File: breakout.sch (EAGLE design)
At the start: 5 parts

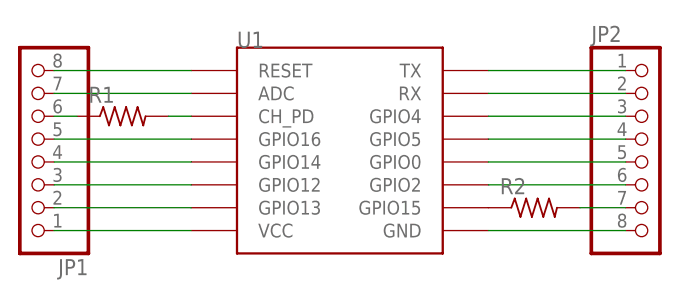
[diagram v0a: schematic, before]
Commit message: Added GPIO0 resistor
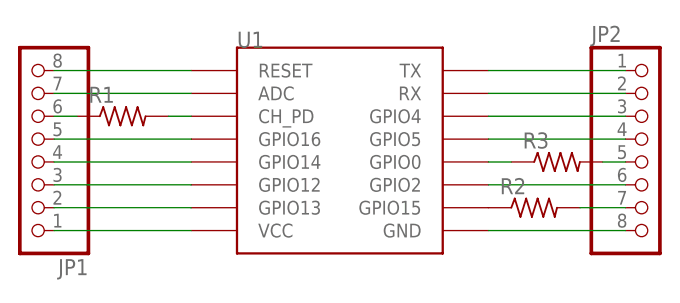
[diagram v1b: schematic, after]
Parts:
- added R3: (no value), resistor:R-US_R0805
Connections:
- new net N$19: JP2.5, R3.2
- net N$13: now also R3.1; no longer JP2.5
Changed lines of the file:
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@@
 <part name="R1" library="resistor" deviceset="R-US_" device="R0805"/>
 <part name="R2" library="resistor" deviceset="R-US_" device="R0805"/>
+<part name="R3" library="resistor" deviceset="R-US_" device="R0805"/>
 </parts>
 <sheets>
@@
 <attribute name="NAME" x="72.39" y="44.6786" size="1.778" layer="95"/>
 <attribute name="VALUE" x="72.39" y="39.878" size="1.778" layer="96"/>
+</instance>
+<instance part="R3" gate="G$1" x="78.74" y="48.26">
+<attribute name="NAME" x="74.93" y="49.7586" size="1.778" layer="95"/>
+<attribute name="VALUE" x="74.93" y="44.958" size="1.778" layer="96"/>
 </instance>
 </instances>
@@
 </segment>
 </net>
-<net name="N$13" class="0">
-<segment>
-<pinref part="U1" gate="G$1" pin="GPIO0"/>
-<pinref part="JP2" gate="A" pin="5"/>
-<wire x1="86.36" y1="48.26" x2="71.12" y2="48.26" width="0.1524" layer="91"/>
-</segment>
-</net>
 <net name="N$14" class="0">
 <segment>
@@
 </segment>
 </net>
+<net name="N$13" class="0">
+<segment>
+<pinref part="U1" gate="G$1" pin="GPIO0"/>
+<pinref part="R3" gate="G$1" pin="1"/>
+<wire x1="73.66" y1="48.26" x2="71.12" y2="48.26" width="0.1524" layer="91"/>
+</segment>
+</net>
+<net name="N$19" class="0">
+<segment>
+<pinref part="JP2" gate="A" pin="5"/>
+<pinref part="R3" gate="G$1" pin="2"/>
+<wire x1="83.82" y1="48.26" x2="86.36" y2="48.26" width="0.1524" layer="91"/>
+</segment>
+</net>

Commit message: Modified pads, changed traces width and gcode options
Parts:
- JP1, JP2: device pinhead:PINHD-1X8 -> pinhead-1:PINHD-1X8_2.54
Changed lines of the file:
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@@
 <grid distance="0.1" unitdist="inch" unit="inch" style="lines" multiple="1" display="no" altdistance="0.01" altunitdist="inch" altunit="inch"/>
 <layers>
-<layer number="1" name="Top" color="4" fill="1" visible="no" active="no"/>
-<layer number="2" name="Route2" color="1" fill="3" visible="no" active="no"/>
-<layer number="3" name="Route3" color="4" fill="3" visible="no" active="no"/>
-<layer number="4" name="Route4" color="1" fill="4" visible="no" active="no"/>
-<layer number="5" name="Route5" color="4" fill="4" visible="no" active="no"/>
-<layer number="6" name="Route6" color="1" fill="8" visible="no" active="no"/>
-<layer number="7" name="Route7" color="4" fill="8" visible="no" active="no"/>
-<layer number="8" name="Route8" color="1" fill="2" visible="no" active="no"/>
-<layer number="9" name="Route9" color="4" fill="2" visible="no" active="no"/>
-<layer number="10" name="Route10" color="1" fill="7" visible="no" active="no"/>
-<layer number="11" name="Route11" color="4" fill="7" visible="no" active="no"/>
-<layer number="12" name="Route12" color="1" fill="5" visible="no" active="no"/>
-<layer number="13" name="Route13" color="4" fill="5" visible="no" active="no"/>
-<layer number="14" name="Route14" color="1" fill="6" visible="no" active="no"/>
-<layer number="15" name="Route15" color="4" fill="6" visible="no" active="no"/>
-<layer number="16" name="Bottom" color="1" fill="1" visible="no" active="no"/>
-<layer number="17" name="Pads" color="2" fill="1" visible="no" active="no"/>
-<layer number="18" name="Vias" color="2" fill="1" visible="no" active="no"/>
-<layer number="19" name="Unrouted" color="6" fill="1" visible="no" active="no"/>
-<layer number="20" name="Dimension" color="15" fill="1" visible="no" active="no"/>
-<layer number="21" name="tPlace" color="7" fill="1" visible="no" active="no"/>
-<layer number="22" name="bPlace" color="7" fill="1" visible="no" active="no"/>
-<layer number="23" name="tOrigins" color="15" fill="1" visible="no" active="no"/>
-<layer number="24" name="bOrigins" color="15" fill="1" visible="no" active="no"/>
-<layer number="25" name="tNames" color="7" fill="1" visible="no" active="no"/>
-<layer number="26" name="bNames" color="7" fill="1" visible="no" active="no"/>
-<layer number="27" name="tValues" color="7" fill="1" visible="no" active="no"/>
-<layer number="28" name="bValues" color="7" fill="1" visible="no" active="no"/>
+<layer number="1" name="Top" color="4" fill="1" visible="yes" active="no"/>
+<layer number="2" name="Route2" color="16" fill="1" visible="yes" active="no"/>
+<layer number="3" name="Route3" color="17" fill="1" visible="yes" active="no"/>
+<layer number="4" name="Route4" color="18" fill="1" visible="yes" active="no"/>
+<layer number="5" name="Route5" color="19" fill="1" visible="yes" active="no"/>
+<layer number="6" name="Route6" color="25" fill="1" visible="yes" active="no"/>
+<layer number="7" name="Route7" color="26" fill="1" visible="yes" active="no"/>
+<layer number="8" name="Route8" color="27" fill="1" visible="yes" active="no"/>
+<layer number="9" name="Route9" color="28" fill="1" visible="yes" active="no"/>
+<layer number="10" name="Route10" color="29" fill="1" visible="yes" active="no"/>
+<layer number="11" name="Route11" color="30" fill="1" visible="yes" active="no"/>
+<layer number="12" name="Route12" color="20" fill="1" visible="yes" active="no"/>
+<layer number="13" name="Route13" color="21" fill="1" visible="yes" active="no"/>
+<layer number="14" name="Route14" color="22" fill="1" visible="yes" active="no"/>
+<layer number="15" name="Route15" color="23" fill="1" visible="yes" active="no"/>
+<layer number="16" name="Bottom" color="1" fill="1" visible="yes" active="no"/>
+<layer number="17" name="Pads" color="2" fill="1" visible="yes" active="no"/>
+<layer number="18" name="Vias" color="2" fill="1" visible="yes" active="no"/>
+<layer number="19" name="Unrouted" color="6" fill="1" visible="yes" active="no"/>
+<layer number="20" name="Dimension" color="24" fill="1" visible="yes" active="no"/>
+<layer number="21" name="tPlace" color="7" fill="1" visible="yes" active="no"/>
+<layer number="22" name="bPlace" color="7" fill="1" visible="yes" active="no"/>
+<layer number="23" name="tOrigins" color="15" fill="1" visible="yes" active="no"/>
+<layer number="24" name="bOrigins" color="15" fill="1" visible="yes" active="no"/>
+<layer number="25" name="tNames" color="7" fill="1" visible="yes" active="no"/>
+<layer number="26" name="bNames" color="7" fill="1" visible="yes" active="no"/>
+<layer number="27" name="tValues" color="7" fill="1" visible="yes" active="no"/>
+<layer number="28" name="bValues" color="7" fill="1" visible="yes" active="no"/>
 <layer number="29" name="tStop" color="7" fill="3" visible="no" active="no"/>
 <layer number="30" name="bStop" color="7" fill="6" visible="no" active="no"/>
@@
 <layer number="35" name="tGlue" color="7" fill="4" visible="no" active="no"/>
 <layer number="36" name="bGlue" color="7" fill="5" visible="no" active="no"/>
-<layer number="37" name="tTest" color="7" fill="1" visible="no" active="no"/>
-<layer number="38" name="bTest" color="7" fill="1" visible="no" active="no"/>
+<layer number="37" name="tTest" color="7" fill="1" visible="yes" active="no"/>
+<layer number="38" name="bTest" color="7" fill="1" visible="yes" active="no"/>
 <layer number="39" name="tKeepout" color="4" fill="11" visible="no" active="no"/>
 <layer number="40" name="bKeepout" color="1" fill="11" visible="no" active="no"/>
@@
 <layer number="44" name="Drills" color="7" fill="1" visible="no" active="no"/>
 <layer number="45" name="Holes" color="7" fill="1" visible="no" active="no"/>
-<layer number="46" name="Milling" color="3" fill="1" visible="no" active="no"/>
-<layer number="47" name="Measures" color="7" fill="1" visible="no" active="no"/>
-<layer number="48" name="Document" color="7" fill="1" visible="no" active="no"/>
-<layer number="49" name="Reference" color="7" fill="1" visible="no" active="no"/>
-<layer number="51" name="tDocu" color="7" fill="1" visible="no" active="no"/>
-<layer number="52" name="bDocu" color="7" fill="1" visible="no" active="no"/>
+<layer number="46" name="Milling" color="3" fill="1" visible="yes" active="no"/>
+<layer number="47" name="Measures" color="7" fill="1" visible="yes" active="no"/>
+<layer number="48" name="Document" color="7" fill="1" visible="yes" active="no"/>
+<layer number="49" name="Reference" color="7" fill="1" visible="yes" active="no"/>
+<layer number="51" name="tDocu" color="7" fill="1" visible="yes" active="no"/>
+<layer number="52" name="bDocu" color="7" fill="1" visible="yes" active="no"/>
 <layer number="88" name="SimResults" color="9" fill="1" visible="yes" active="yes"/>
 <layer number="89" name="SimProbes" color="9" fill="1" visible="yes" active="yes"/>
@@
 <parts>
 <part name="U1" library="esp8266modules" deviceset="ESP12" device="SMD"/>
-<part name="JP1" library="pinhead" library_urn="urn:adsk.eagle:library:325" deviceset="PINHD-1X8" device="" package3d_urn="urn:adsk.eagle:package:22409/2"/>
-<part name="JP2" library="pinhead" library_urn="urn:adsk.eagle:library:325" deviceset="PINHD-1X8" device="" package3d_urn="urn:adsk.eagle:package:22409/2"/>
+<part name="JP1" library="pinhead-1" deviceset="PINHD-1X8" device="_2.54"/>
+<part name="JP2" library="pinhead-1" deviceset="PINHD-1X8" device="_2.54"/>
 <part name="R1" library="resistor" deviceset="R-US_" device="R0805"/>
 <part name="R2" library="resistor" deviceset="R-US_" device="R0805"/>
@@
 </segment>
 </net>
-<net name="N$6" class="0">
-<segment>
-<pinref part="JP2" gate="A" pin="7"/>
-<wire x1="86.36" y1="43.18" x2="81.28" y2="43.18" width="0.1524" layer="91"/>
-<pinref part="R2" gate="G$1" pin="2"/>
-</segment>
-</net>
 <net name="N$15" class="0">
 <segment>
@@
 <pinref part="R3" gate="G$1" pin="2"/>
 <wire x1="83.82" y1="48.26" x2="86.36" y2="48.26" width="0.1524" layer="91"/>
+</segment>
+</net>
+<net name="N$20" class="0">
+<segment>
+<pinref part="R2" gate="G$1" pin="2"/>
+<pinref part="JP2" gate="A" pin="7"/>
+<wire x1="86.36" y1="43.18" x2="81.28" y2="43.18" width="0.1524" layer="91"/>
 </segment>
 </net>
@@
 </schematic>
 </drawing>
-<compatibility>
-<note version="8.2" severity="warning">
-Since Version 8.2, EAGLE supports online libraries. The ids
-of those online libraries will not be understood (or retained)
-with this version.
-</note>
-<note version="8.3" severity="warning">
-Since Version 8.3, EAGLE supports URNs for individual library
-assets (packages, symbols, and devices). The URNs of those assets
-will not be understood (or retained) with this version.
-</note>
-<note version="8.3" severity="warning">
-Since Version 8.3, EAGLE supports the association of 3D packages
-with devices in libraries, schematics, and board files. Those 3D
-packages will not be understood (or retained) with this version.
-</note>
-</compatibility>
 </eagle>
